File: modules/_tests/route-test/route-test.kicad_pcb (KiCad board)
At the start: 2 copper layers, 40 x 32 mm, 8 parts, among them J1 LEFT, J2 RIGHT

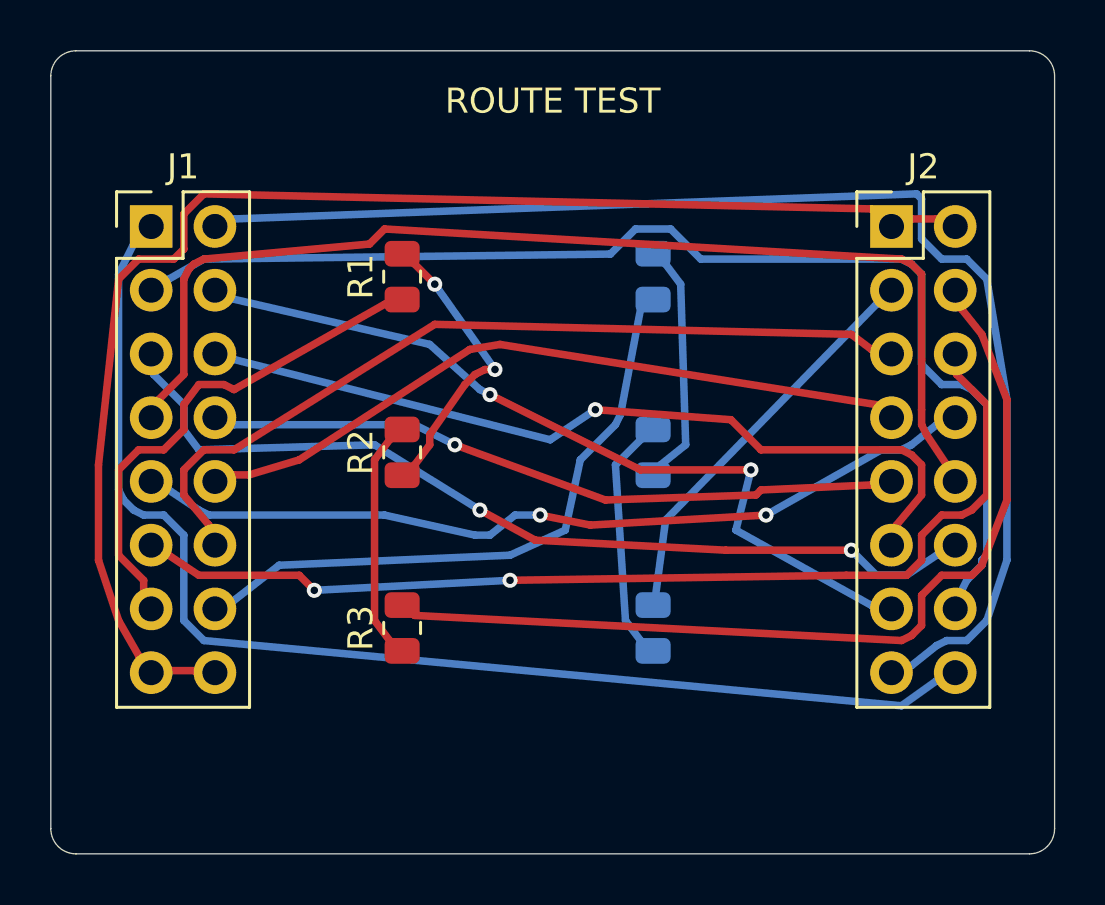
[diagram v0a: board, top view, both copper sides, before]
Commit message: Router: mutable-array A*, reroute only contested nets, octile heuristic, score report
A* now runs in ST over unboxed arrays with a binary heap and a flattened
per-net penalty array instead of immutable Set/IntMap churn (175 GB of
allocation on the stress test). After iteration one only nets that are
in conflict are ripped up; the sharing penalty grows 1.4x per iteration.
Stress test: 86 s -> 3 s CPU, 38 -> 19 iterations, DRC still clean.

pcbgen writes modules/<name>/route-report.md: per-net segments, vias,
length and detour ratio against the Euclidean MST of the pads, so routing
quality is diffable across commits. -O2 and -rtsopts enabled.

Co-Authored-By: Claude Fable 5.1 <noreply@anthropic.com>
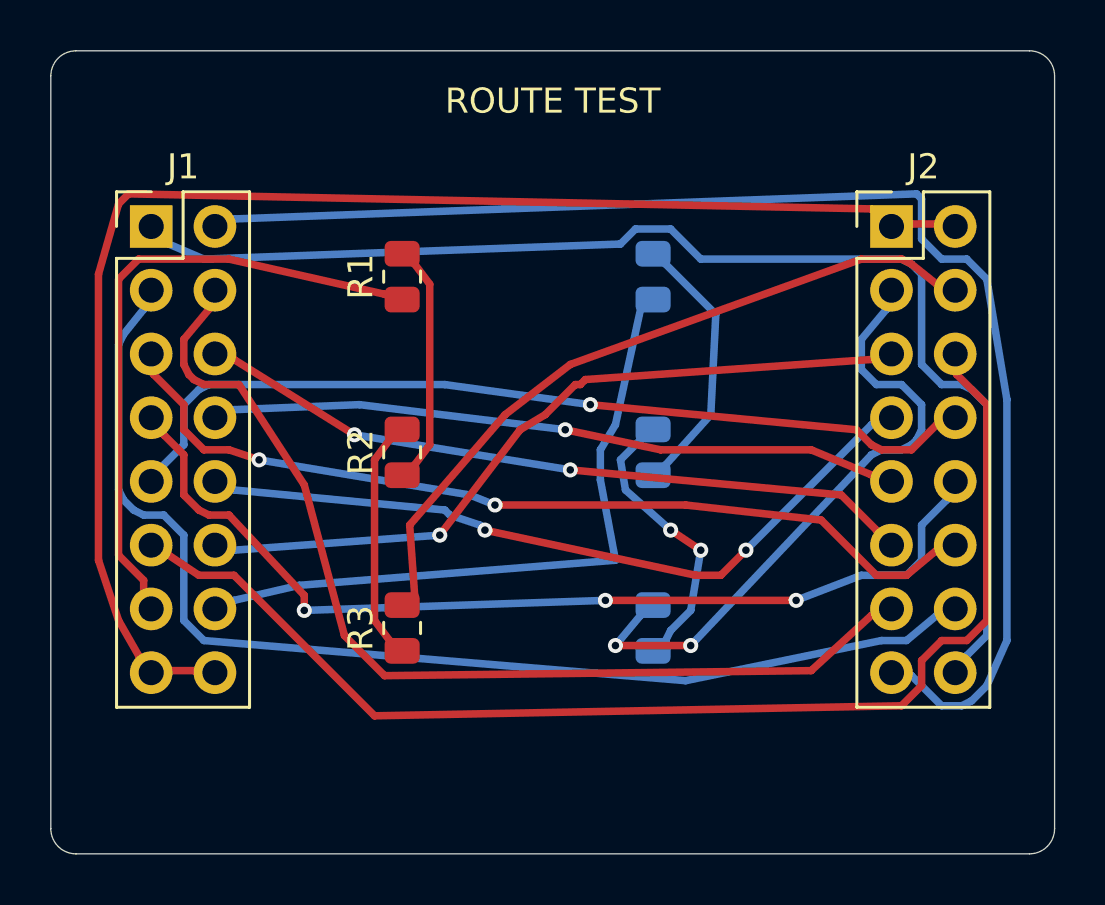
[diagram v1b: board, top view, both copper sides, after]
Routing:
- net /RH: track 16.3 -> 25.6 mm, vias 0 -> 2
- net /RD: track 36.8 -> 29.0 mm
- net /X4: track 32.6 -> 40.3 mm, vias 2 -> 0
- net /X11: track 41.9 -> 49.1 mm, vias 2 -> 0
- net /X7: track 44.9 -> 39.3 mm, vias 0 -> 3
- net /RA: track 20.3 -> 25.4 mm
- net /X6: track 33.3 -> 28.8 mm, vias 1 -> 2
- net /X12: track 33.6 -> 29.9 mm, vias 0 -> 1
- net /X2: track 51.5 -> 54.2 mm
- net /RE: track 24.9 -> 27.1 mm
- net /RB: track 11.8 -> 9.70 mm, vias 2 -> 0
- net /RG: track 9.92 -> 11.5 mm, vias 0 -> 2
- net /X9: track 33.9 -> 35.5 mm, vias 2 -> 1
- net /X10: track 28.8 -> 30.0 mm, vias 0 -> 2
- net /RF: track 9.84 -> 10.8 mm
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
